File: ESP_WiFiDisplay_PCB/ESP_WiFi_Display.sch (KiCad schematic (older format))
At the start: 25 parts, among them P1 SERIAL_HC12, P2 USB, P3 NODEMCU_1, P4 NODEMCU_2, P5 LOCAL 5V?, P6 WS2812 LED, P7 PCB, P8 LOGO1, P9 LOGO2, SW1 SWUP, SW2 SWDOWN, SW3 ON/OFF, U1 NODEMCU, U3 74LVC1G17

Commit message: Update of Readme and PCB changed
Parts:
- removed D2: A, REInnovationFootprint:TH_LED-5MM_larg_pad, symbol LED-RESCUE-MiniPredictionMachine_WIFI_Unit
- removed P5: LOCAL 5V?, matts_components:SIL-2_solder_connect, symbol CONN_01X02
- removed R1: 330, REInnovationFootprint:TH_Resistor_1, symbol R
- removed R3, R4: 10k, REInnovationFootprint:TH_Resistor_1, symbol R
- removed SW1: SWUP, REInnovationFootprint:SW_PUSH_SMALL_lg_pad, symbol SW_PUSH_SMALL_H
- removed SW2: SWDOWN, REInnovationFootprint:SW_PUSH_SMALL_lg_pad, symbol SW_PUSH_SMALL_H
- added D4, D5, D6, D7: WS2812, REInnovationFootprint:TH_WS2811_LED_8mm, symbol WS2811_EpiStar_8mm
- added ENC1: Encoder_1, matts_components:Encoder, symbol Encoder_1
- D3: renamed from D1; value WS2811_EpiStar_8mm -> WS2812
- P9: renamed from P6; value WS2812 LED -> S_SERIAL
- gave numbers to parts that had none: 1
- renumbered D5 to D1, D3 to D2, P2 to P1, P7 to P5, P8 to P6, P9 to P7, P1 to P8, R2 to R1, SW3 to SW1, U3 to U2
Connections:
- net SW_UP is gone; now on net HC12_SET: P4.15 (P15), U1.30 (D0)
- net +3V3: now also P9.4 (P4)
- net 5V_PWR: now also D4.2 (+Vin), D5.2 (+Vin), D6.2 (+Vin), D7.2 (+Vin)
- net GND: now also P9.1 (P1), D4.3 (GND), D5.3 (GND), D6.3 (GND), D7.3 (GND), ENC1.2, ENC1.C; no longer P9.4 (P4)
- net HC12_SET: no longer P4.14 (P14), U1.29 (D1)
- net SOFT_Rx: now also P9.2 (P2)
- net at D3.4 (DATA_IN), U2.4 (Y): no longer P9.3 (P3)
- net at D3.1 (DATA_OUT): now also D4.4 (DATA_IN)
- net at D1.2 (A), P1.1 (VCC): now also P2.1 (VCC)
- net LED_A renamed SW_ENC
- net SW_ENC: now also ENC1.1
- net SOFT_Tx renamed ENC_A
- net ENC_A: now also P9.3 (P3), ENC1.A
- new net: D4.1 (DATA_OUT), D5.4 (DATA_IN)
- new net: D5.1 (DATA_OUT), D6.4 (DATA_IN)
- new net: D6.1 (DATA_OUT), D7.4 (DATA_IN)
- new net ENC_B: ENC1.B, P4.14 (P14), U1.29 (D1)
- no-connect marks 5 -> 4
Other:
- moved on the sheet: D2, D3, DISP1, P3, P4, P5, P6, P7, P8, P9, R1, U1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

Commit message: PCB changes
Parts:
- removed P1: USB, REInnovationFootprint:TH_USB_B_lg_pad, symbol USB_B-RESCUE-MiniPredictionMachine_WIFI_Unit
- added C1, C2, C3, C4, C5: 100n, matts_components:C1_wide_lg_pad, symbol C
- added P1: USB_Micro, REInnovationFootprint:USB_Micro-B_MOLEX_47642-0001, symbol USB_Micro
- added P10: 5V_EXT, REInnovationFootprint:TH_CONN_2W, symbol CONN_01X02
- D3, D4, D5, D6, D7: footprint REInnovationFootprint:TH_WS2811_LED_8mm -> LEDs:LED_WS2812B-PLCC4
- U1: Description (none) -> Node MCU Amica version. ESP8266 breakout.
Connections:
- net 5V_PWR: now also C1.1, C2.1, C3.1, C4.1, C5.1
- net GND: now also C1.2, C2.2, C3.2, C4.2, C5.2, P1.5 (GND), P10.2 (P2)
- net at D1.2 (A), P2.1 (VCC): now also P1.1 (VCC), P10.1 (P1)
- no-connect marks 4 -> 8
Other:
- note added: "External 5V\n"
- note added: "Micro USB"
- note added: "USB B\n"
- note removed: "USB input USB-B_1"
- note removed: "USB input USB-B_2\n"

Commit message: Small PCB changes
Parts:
- removed P2: USB, REInnovationFootprint:TH_USB_B_lg_pad, symbol USB_B-RESCUE-MiniPredictionMachine_WIFI_Unit
- added D2: 1N5819, REInnovationFootprint:TH_Diode_1, symbol D_Schottky
- D1: value D_Schottky -> 1N5819; Description (none) -> 1A Schottky diode; Manufacturer (none) -> HY Electronic Corp; Supplier 1 (none) -> RS; Supplier 1 Cost (none) -> 0.02; Supplier 1 Part No (none) -> 917-9108
- D8: renamed from D2; value B -> LED
- ENC1: value Encoder_1 -> Encoder
- P8: footprint REInnovationFootprint:TH_SIL_5_1mm -> REInnovationFootprint:TH_SIL_5_HC12
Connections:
- net at D1.1 (K), F1.1: now also D2.1 (K)
- net at D1.2 (A), P1.1 (VCC): no longer P10.1 (P1)
- new net: D2.2 (A), P10.1 (P1)
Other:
- note removed: "USB B\n"
- moved on the sheet: D1, DISP1, F1, P1, P10, SW1

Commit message: PCB initial wiring. Cost and Parts info done
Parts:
- removed D3, D4, D5, D6, D7: WS2812, LEDs:LED_WS2812B-PLCC4, symbol WS2811_EpiStar_8mm
- added D3, D4, D5, D6, D7: WS2812B_SMD, REInnovationFootprint:SM_WS2812B, symbol WS2812B_SMD
- added P8: LOGO_MOUSE, CuriousElectric3:CEC_Globe_10mm_FCU, symbol CONN_01X01
- added P9: HARDWARE, CuriousElectric3:CEC_Globe_10mm_FCU, symbol CONN_01X01
- C1, C2, C3, C4, C5: Supplier 1 (none) -> Rapid; Supplier 1 Cost (none) -> 0.07; Supplier 1 Part No (none) -> 10-3260
- D8: Supplier 1 Cost (none) -> 0.05
- DISP1: Description (none) -> OLED display 128x64 IIC; Supplier 1 (none) -> Aliexpress; Supplier 1 Cost (none) -> 2.75; Supplier 1 Part No (none) -> https://www.aliexpress.com/item/Free-Shipping-10pcs-2015-wh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
- ENC1: footprint matts_components:Encoder -> REInnovationFootprint:TH_Encoder; Description (none) -> Rotary encoder; Supplier 1 (none) -> Aliexpress; Supplier 1 Cost (none) -> 0.50; Supplier 1 Part No (none) -> https://www.aliexpress.com/item/Wholesale-20pcs-lot-12mm-Ro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
- P1: Description (none) -> Micro USB connector; Manufacturer (none) -> MOLEX; Manufacturer Part No (none) -> 47642-0001; Supplier 1 (none) -> RS; Supplier 1 Cost (none) -> 0.60; Supplier 1 Part No (none) -> 896-7419
- P2: renamed from P10; footprint REInnovationFootprint:TH_CONN_2W -> matts_components:SIL-2_screw_terminal; Description (none) -> Screw terminal conenctor; Supplier 1 (none) -> Aliexpress; Supplier 1 Cost (none) -> 0.10
- R1: Supplier 1 Cost (none) -> 0.01
- SW1: Supplier 1 (none) -> Aliexpress; Supplier 1 Cost (none) -> 0.2
- U1: Supplier 1 (none) -> AliExpress; Supplier 1 Cost (none) -> 3.50; Supplier 1 Part No (none) -> https://www.aliexpress.com/item/Update-Industry-4-0-New-esp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
- U2: Manufacturer (none) -> Nexperia; Manufacturer Part No (none) -> 74LVC1G17GV; Supplier 1 (none) -> RS; Supplier 1 Cost (none) -> 0.06; Supplier 1 Part No (none) -> 816-8763
- renumbered P6 to P10, P7 to P11, P8 to P3, P9 to P4, P3 to P5, P4 to P6, P5 to P7
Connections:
- net 5V_PWR: now also D3.1 (+V), D4.1 (+V), D5.1 (+V), D6.1 (+V), D7.1 (+V)
- net GND: now also D3.3 (GND), D4.3 (GND), D5.3 (GND), D6.3 (GND), D7.3 (GND)
- net at U2.4 (Y): now also D3.4 (D_IN)
- new net: D3.2 (D_OUT), D4.4 (D_IN)
- new net: D4.2 (D_OUT), D5.4 (D_IN)
- new net: D5.2 (D_OUT), D6.4 (D_IN)
- new net: D6.2 (D_OUT), D7.4 (D_IN)
- no-connect marks 8 -> 11
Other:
- moved on the sheet: P10, P11, P5, P6, P7, U1

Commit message: Full review of boards - needs NAME still!
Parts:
- added P12: KNOB, CuriousElectric3:CEC_Globe_10mm_FCU, symbol CONN_01X01
- D3: Supplier 1 Part No https://www.aliexpress.com/item/10-1000pcs-WS2812B-4pins-5050-SMD-Black-White-version-WS2812-Individually-Addressable-Digital-RGB-LED-Chip/ -> https://www.aliexpress.com/item/10-1000pcs-WS2812B-4pins-5050-SMD-Black-White-version-WS2812-Individually-Addressable-Digital-RGB-LED-Chip/32453497583.html
- P8: footprint CuriousElectric3:CEC_Globe_10mm_FCU -> CuriousElectric3:mouse10x10
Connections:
- no-connect marks 11 -> 12
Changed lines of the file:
@@
 F 0 "P8" H 6700 5900 50  0000 C CNN
 F 1 "LOGO_MOUSE" V 6800 5800 50  0000 C CNN
-F 2 "CuriousElectric3:CEC_Globe_10mm_FCU" H 6700 5800 50  0001 C CNN
+F 2 "CuriousElectric3:mouse10x10" H 6700 5800 50  0001 C CNN
 F 3 "" H 6700 5800 50  0000 C CNN
 	1    6700 5800
@@
 F 7 "~" H 6300 3500 60  0001 C CNN "Manufacturer Part No"
 F 8 "AliExpress" H 6300 3500 60  0001 C CNN "Supplier 1"
-F 9 "https://www.aliexpress.com/item/10-1000pcs-WS2812B-4pins-5050-SMD-Black-White-version-WS2812-Individually-Addressable-Digital-RGB-LED-Chip/" H 6300 3500 60  0001 C CNN "Supplier 1 Part No"
+F 9 "https://www.aliexpress.com/item/10-1000pcs-WS2812B-4pins-5050-SMD-Black-White-version-WS2812-Individually-Addressable-Digital-RGB-LED-Chip/32453497583.html" H 6300 3500 60  0001 C CNN "Supplier 1 Part No"
 F 10 "0.10" H 6300 3500 60  0001 C CNN "Supplier 1 Cost"
 F 11 "~" H 6300 3500 60  0001 C CNN "Supplier 2"
@@
 	-1   0    0    1
 $EndComp
+$Comp
+L CONN_01X01 P12
+U 1 1 598DB6BF
+P 9800 1750
+F 0 "P12" H 9800 1850 50  0000 C CNN
+F 1 "KNOB" V 9900 1750 50  0000 C CNN
+F 2 "CuriousElectric3:CEC_Globe_10mm_FCU" H 9800 1750 50  0001 C CNN
+F 3 "" H 9800 1750 50  0000 C CNN
+	1    9800 1750
+	1    0    0    -1
+$EndComp
+NoConn ~ 9600 1750
 $EndSCHEMATC

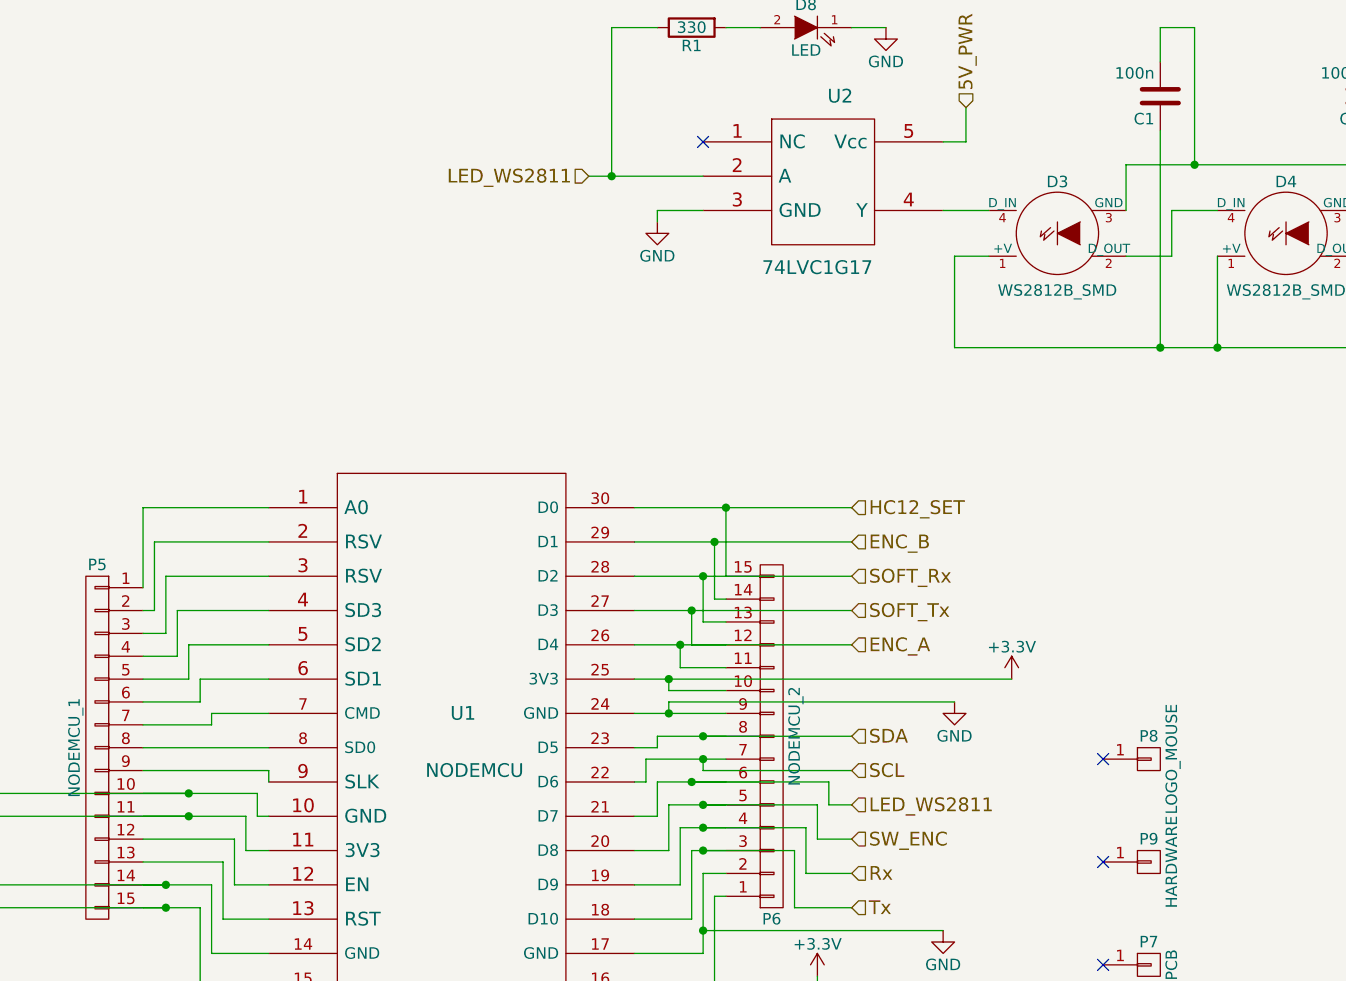
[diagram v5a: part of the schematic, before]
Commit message: Updated PCB with name
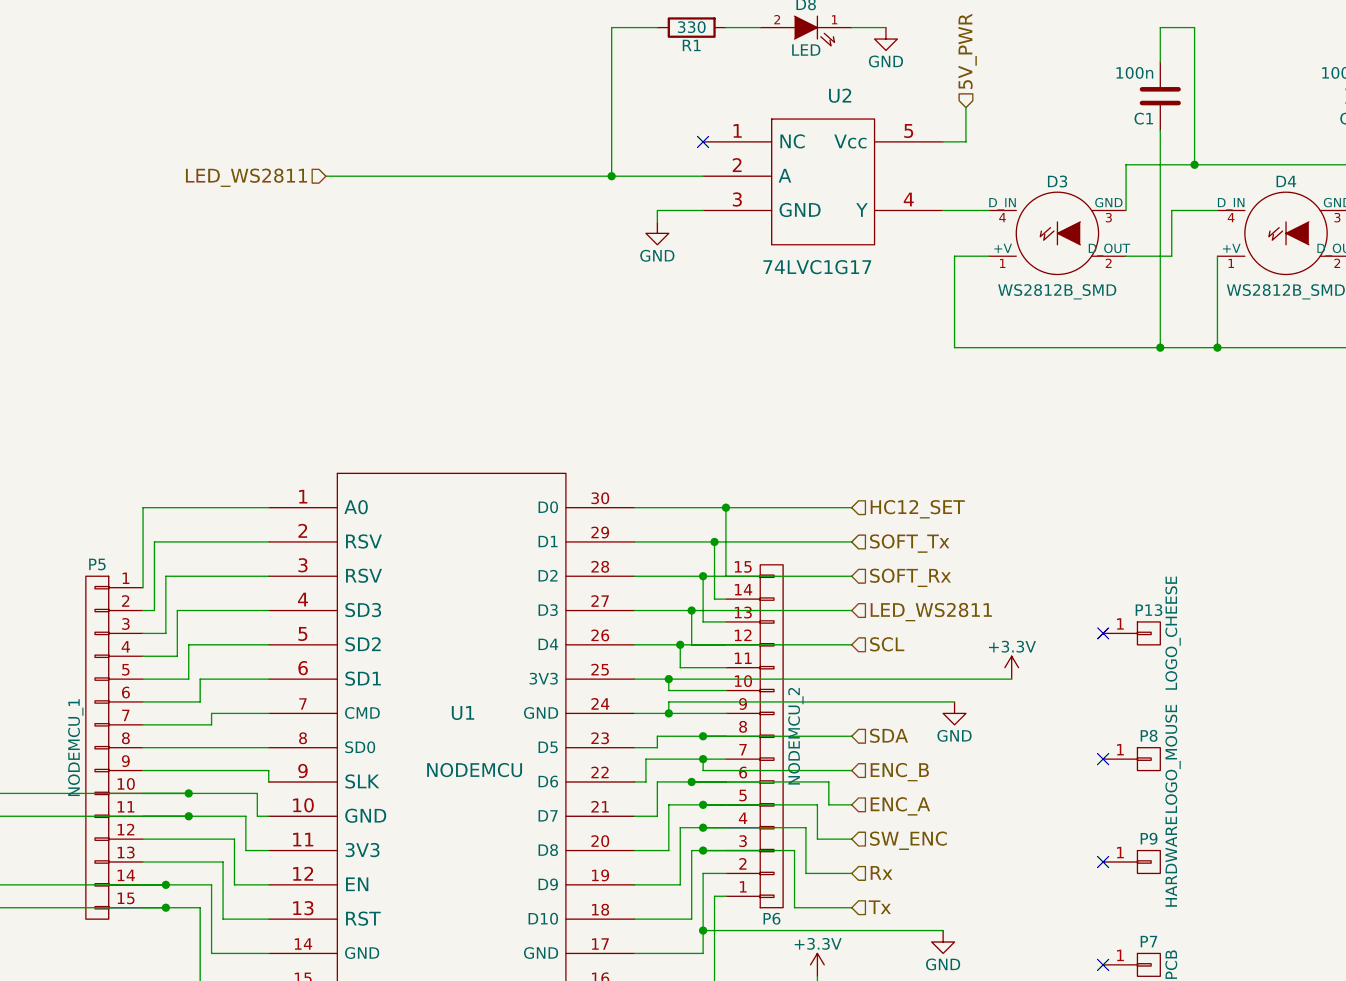
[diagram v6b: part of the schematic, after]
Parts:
- added P13: LOGO_CHEESE, CuriousElectric3:CheeseWedge8mm, symbol CONN_01X01
- P12, P9: footprint CuriousElectric3:CEC_Globe_10mm_FCU -> (none)
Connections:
- net ENC_A: now also P6.6 (P6), U1.21 (D7); no longer P3.3 (P3), P4.3 (P3), P6.11 (P11), P6.12 (P12), U1.26 (D4), U1.27 (D3)
- net ENC_B: now also P6.7 (P7), U1.22 (D6); no longer P6.14 (P14), U1.29 (D1)
- net LED_WS2811: now also DISP1.2 (SCL), P6.11 (P11), P6.12 (P12), U1.26 (D4), U1.27 (D3); no longer P6.6 (P6), U1.21 (D7)
- removed net SCL: DISP1.2 (SCL), P6.7 (P7), U1.22 (D6)
- new net SOFT_Tx: P3.3 (P3), P4.3 (P3), P6.14 (P14), U1.29 (D1)
- no-connect marks 12 -> 13
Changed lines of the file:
@@
 	1    0    0    -1
 $EndComp
-Text HLabel 4250 3250 0    60   Input ~ 0
+Text HLabel 3100 3250 0    60   Input ~ 0
 LED_WS2811
 $Comp
@@
 Wire Wire Line
 	4350 2600 4550 2600
-Text HLabel 5400 6000 2    60   Input ~ 0
+Text HLabel 5400 5150 2    60   Input ~ 0
 LED_WS2811
 Text HLabel 5400 5700 2    60   Input ~ 0
 SDA
-Text HLabel 5400 5850 2    60   Input ~ 0
+Text HLabel 5400 5300 2    60   Input ~ 0
 SCL
 $Comp
@@
 Text HLabel 7250 1400 0    60   Input ~ 0
 SCL
-Text HLabel 5400 5150 2    60   Input ~ 0
+Text HLabel 5400 4850 2    60   Input ~ 0
 SOFT_Tx
 Text HLabel 5400 5000 2    60   Input ~ 0
@@
 Wire Wire Line
 	4650 5400 4650 5300
-Wire Wire Line
-	4450 5300 5400 5300
 Wire Wire Line
 	4850 5500 4600 5500
@@
 	1    0    0    -1
 $EndComp
-Text HLabel 5400 5300 2    60   Input ~ 0
+Text HLabel 5400 6000 2    60   Input ~ 0
 ENC_A
-Text HLabel 5400 4850 2    60   Input ~ 0
+Text HLabel 5400 5850 2    60   Input ~ 0
 ENC_B
 Text HLabel 5400 6150 2    60   Input ~ 0
@@
 	10750 1550 10750 1250
 Wire Wire Line
-	4250 3250 4750 3250
+	3100 3250 4750 3250
 Wire Wire Line
 	6000 3600 5850 3600
@@
 F 0 "P9" H 6700 6350 50  0000 C CNN
 F 1 "HARDWARE" V 6800 6250 50  0000 C CNN
-F 2 "CuriousElectric3:CEC_Globe_10mm_FCU" H 6700 6250 50  0001 C CNN
+F 2 "" H 6700 6250 50  0001 C CNN
 F 3 "" H 6700 6250 50  0000 C CNN
+F 4 "~" H 6700 6250 60  0000 C CNN "Notes"
+F 5 "~" H 6700 6250 60  0001 C CNN "Description"
+F 6 "~" H 6700 6250 60  0001 C CNN "Manufacturer"
+F 7 "~" H 6700 6250 60  0001 C CNN "Manufacturer Part No"
+F 8 "~" H 6700 6250 60  0001 C CNN "Supplier 1"
+F 9 "~" H 6700 6250 60  0001 C CNN "Supplier 1 Part No"
+F 10 "~" H 6700 6250 60  0001 C CNN "Supplier 1 Cost"
+F 11 "~" H 6700 6250 60  0001 C CNN "Supplier 2"
+F 12 "~" H 6700 6250 60  0001 C CNN "Supplier 2 Part No"
+F 13 "~" H 6700 6250 60  0001 C CNN "Supplier 2 Cost"
 	1    6700 6250
 	1    0    0    -1
@@
 F 0 "P12" H 9800 1850 50  0000 C CNN
 F 1 "KNOB" V 9900 1750 50  0000 C CNN
-F 2 "CuriousElectric3:CEC_Globe_10mm_FCU" H 9800 1750 50  0001 C CNN
+F 2 "" H 9800 1750 50  0001 C CNN
 F 3 "" H 9800 1750 50  0000 C CNN
+F 4 "~" H 9800 1750 60  0000 C CNN "Notes"
+F 5 "~" H 9800 1750 60  0001 C CNN "Description"
+F 6 "~" H 9800 1750 60  0001 C CNN "Manufacturer"
+F 7 "~" H 9800 1750 60  0001 C CNN "Manufacturer Part No"
+F 8 "~" H 9800 1750 60  0001 C CNN "Supplier 1"
+F 9 "~" H 9800 1750 60  0001 C CNN "Supplier 1 Part No"
+F 10 "~" H 9800 1750 60  0001 C CNN "Supplier 1 Cost"
+F 11 "~" H 9800 1750 60  0001 C CNN "Supplier 2"
+F 12 "~" H 9800 1750 60  0001 C CNN "Supplier 2 Part No"
+F 13 "~" H 9800 1750 60  0001 C CNN "Supplier 2 Cost"
 	1    9800 1750
 	1    0    0    -1
 $EndComp
 NoConn ~ 9600 1750
+Wire Wire Line
+	4450 5300 5400 5300
+$Comp
+L CONN_01X01 P13
+U 1 1 59AE9868
+P 6700 5250
+F 0 "P13" H 6700 5350 50  0000 C CNN
+F 1 "LOGO_CHEESE" V 6800 5250 50  0000 C CNN
+F 2 "CuriousElectric3:CheeseWedge8mm" H 6700 5250 50  0001 C CNN
+F 3 "" H 6700 5250 50  0000 C CNN
+	1    6700 5250
+	1    0    0    -1
+$EndComp
+NoConn ~ 6500 5250
 $EndSCHEMATC
